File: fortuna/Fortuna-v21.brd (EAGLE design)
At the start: 66 x 55.9 mm, 41 parts, among them J1 5V, J2 GND, J3 A0, J4 A3, J5 A5, J6 D2, J7 *D5, J8 *D10, J9 VIN, M1 MOTOR20MM, M2 MOTOR20MM, Q1 PN2222A, Q2 PN2222A, U1 OPA2344, U2 OPA2344

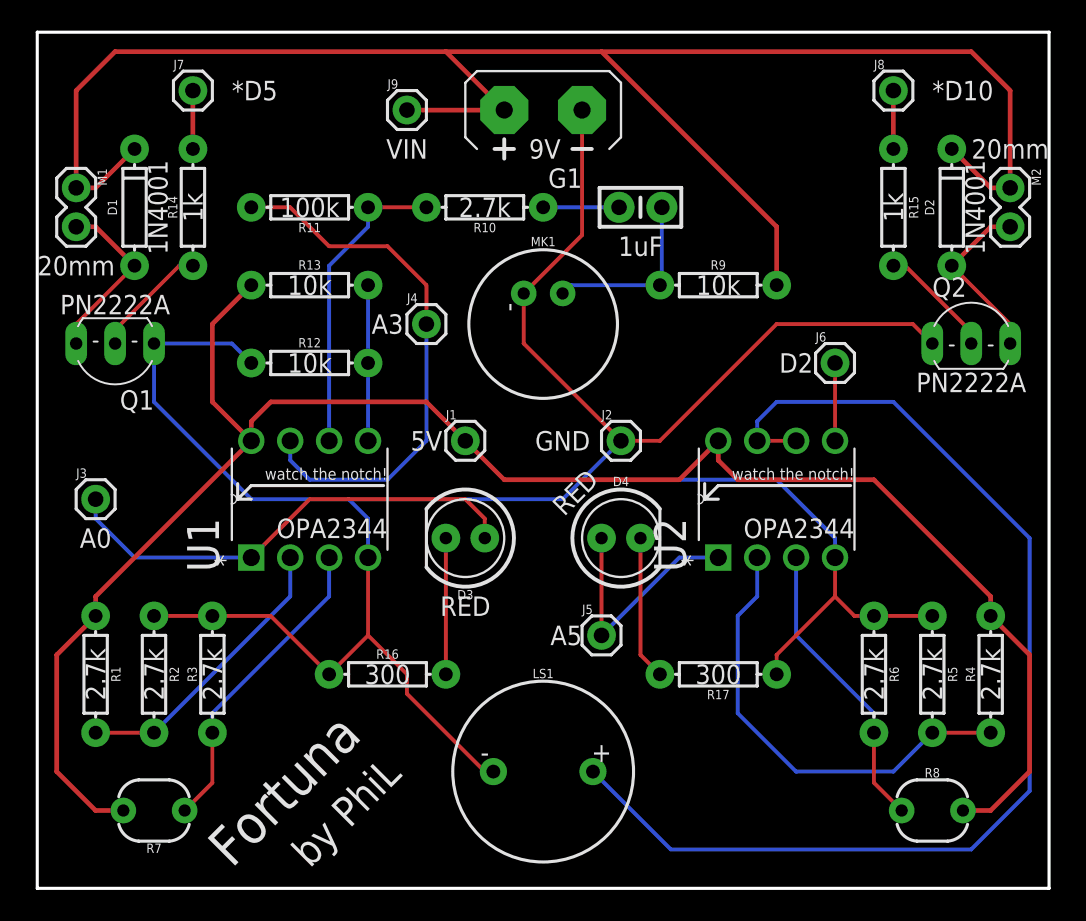
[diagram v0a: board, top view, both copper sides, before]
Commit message: Merge two OPA2344's into one OPA4344 & Add SPDT power switch
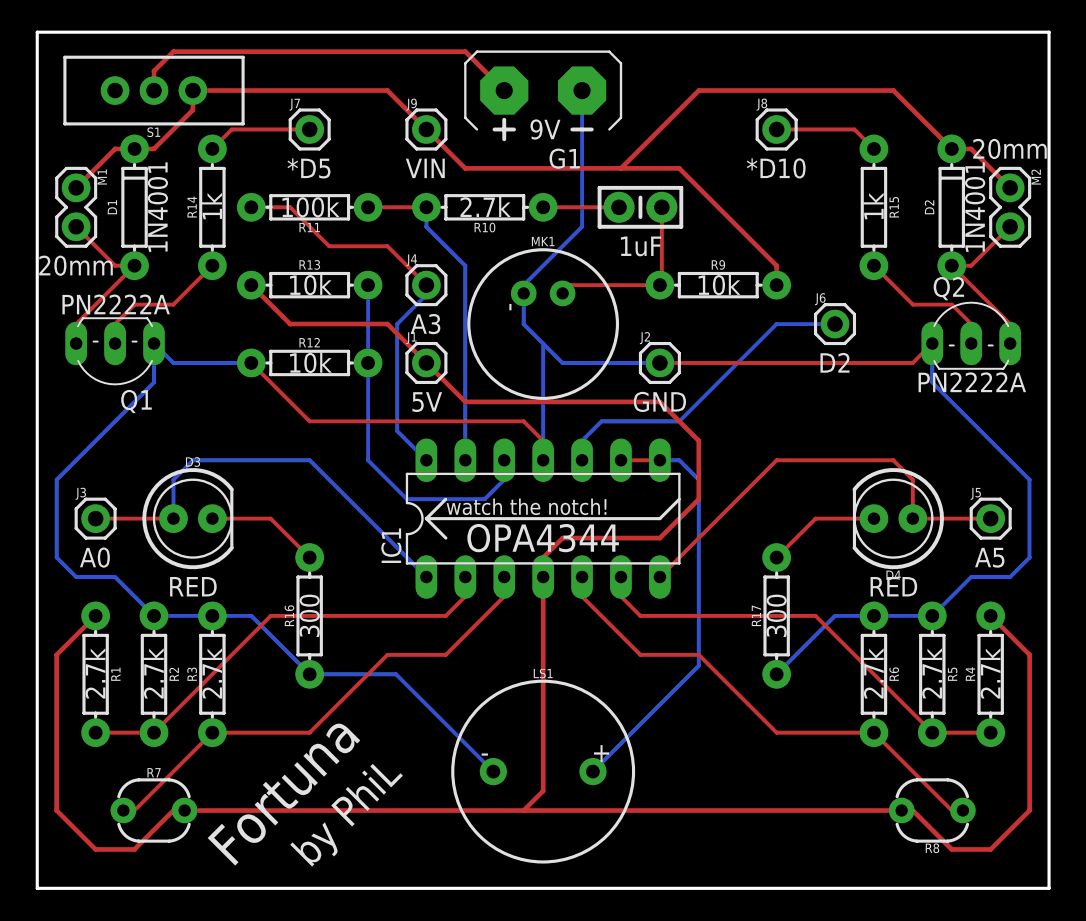
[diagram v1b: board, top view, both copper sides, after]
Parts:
- removed U1, U2: OPA2344, TexasInstruments:DIP254P762X508-8
- added IC1: OPA4340P, burr-brown:DIL14
- added S1: POWER_SWITCH, SparkFun-Switches:SWITCH_SPDT_PTH_11.6X4.0MM
- D1, D2: value 200mA/100V/1V -> 1N4001
- moved J5 26.5 mm to (62.2, 24.1)
- moved D3 17.8 mm to (10.2, 24.1), turned to 0 degrees
- moved D4 17.8 mm to (55.9, 24.1), turned to 180 degrees
- moved J8 8.03 mm to (48.3, 49.5)
- moved J7 8.03 mm to (17.8, 49.5)
- moved R16 6.35 mm to (17.8, 17.8), turned to 90 degrees
- moved J1 5.68 mm to (25.4, 34.3)
- moved J2 5.68 mm to (40.6, 34.3)
- moved R17 5.39 mm to (48.3, 17.8), turned to 90 degrees
- moved J4 2.54 mm to (25.4, 39.4)
- moved J6 2.54 mm to (52.1, 36.8)
- moved J9 1.80 mm to (25.4, 49.5)
- moved G1 1.27 mm to (33.0, 52.1)
- moved R15 1.27 mm to (54.6, 44.5)
- moved J3 1.27 mm to (3.81, 24.1)
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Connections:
- net *D10 renamed OUT_RMOTOR
- net *D5 renamed OUT_LMOTOR
- removed net A0: D3.A, J3.1, U1.1
- removed net A3: J4.1, R11.P$2, U1.7
- removed net A5: D4.A, J5.1, U2.1
- new net 9V: G1.+, S1.2
- new net OUT_LPHOTO: D3.A, IC1.1, J3.1
- new net OUT_MIC: IC1.14, J4.1, R11.P$2
- new net OUT_RPHOTO: D4.A, IC1.7, J5.1
- net +LPHOTO: now also IC1.3; no longer U1.3
- net +MIC: now also IC1.12; no longer U1.5
- net +RPHOTO: now also IC1.5; no longer U2.3
- net -LPHOTO: now also IC1.2; no longer U1.2
- net -MIC: now also IC1.13; no longer U1.6
- net -RPHOTO: now also IC1.6; no longer U2.2
- net 5V: now also IC1.4; no longer U1.8, U2.8
- net D2: now also IC1.10; no longer U2.5
- net GND: now also IC1.11; no longer U1.4, U2.4
- net OUT_BUZZER: now also IC1.8, IC1.9; no longer U2.6, U2.7
- net VIN: now also S1.3; no longer G1.+
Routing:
- net OUT_BUZZER: track 74.5 -> 27.5 mm
- net 5V: track 120.6 -> 161.2 mm
- net A3: track 35.4 -> 0.00 mm
- net VIN: track 117.2 -> 85.2 mm
- net A0: track 31.1 -> 0.00 mm
- net OUT_RPHOTO: track 0.00 -> 27.8 mm
- net OUT_LPHOTO: track 0.00 -> 27.8 mm
- net OUT_MIC: track 0.00 -> 26.5 mm
- net 9V: track 0.00 -> 25.7 mm
- net A5: track 16.1 -> 0.00 mm
- net D2: track 5.08 -> 20.9 mm
- net +MIC: track 10.2 -> 23.2 mm
- net +RPHOTO: track 19.4 -> 31.9 mm
- net +LPHOTO: track 20.4 -> 31.9 mm
- net -LPHOTO: track 18.9 -> 29.1 mm
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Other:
- board text added: "OPA4344"
- board text removed: "OPA2344"

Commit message: Fillet corners of the boards
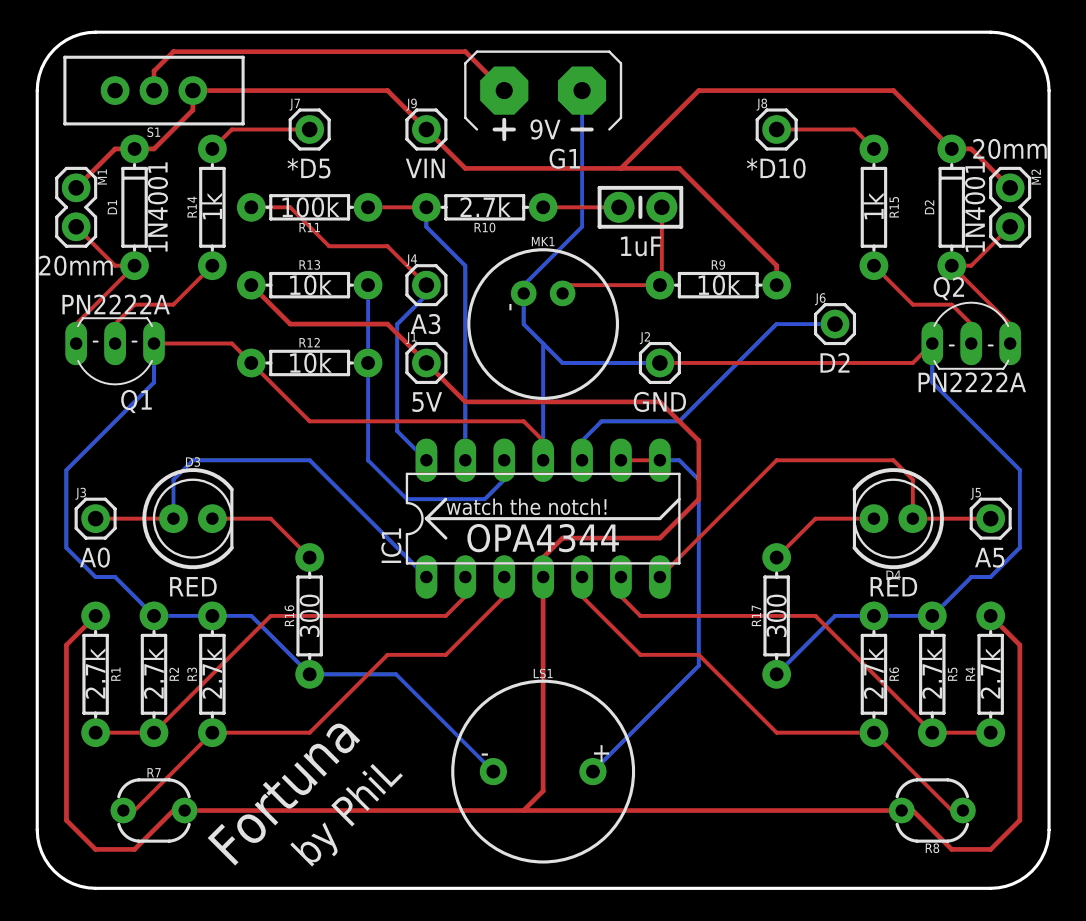
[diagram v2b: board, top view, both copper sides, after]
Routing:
- net GND: track 169.1 -> 166.6 mm
- net 5V: track 161.2 -> 160.2 mm
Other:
- outline, holes or cut-outs redrawn
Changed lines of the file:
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@@
 <board>
 <plain>
-<wire x1="0" y1="0" x2="0" y2="55.88" width="0.2032" layer="20"/>
-<wire x1="0" y1="55.88" x2="66.04" y2="55.88" width="0.2032" layer="20"/>
-<wire x1="66.04" y1="55.88" x2="66.04" y2="0" width="0.2032" layer="20"/>
-<wire x1="66.04" y1="0" x2="0" y2="0" width="0.2032" layer="20"/>
+<wire x1="0" y1="3.81" x2="0" y2="52.07" width="0.2032" layer="20"/>
+<wire x1="3.81" y1="55.88" x2="62.23" y2="55.88" width="0.2032" layer="20"/>
+<wire x1="66.04" y1="52.07" x2="66.04" y2="3.81" width="0.2032" layer="20"/>
 <text x="31.75" y="-7.62" size="1.778" layer="51" font="vector">Phi Luu</text>
 <text x="25.4" y="46.99" size="1.27" layer="21" font="vector" ratio="10" align="center">VIN</text>
@@
 <text x="22.86" y="11.43" size="2.54" layer="22" font="vector" ratio="15" rot="MR315">Fortuna</text>
 <text x="25.4" y="8.89" size="1.9304" layer="22" font="vector" ratio="15" rot="MR315">by PhiL</text>
+<wire x1="62.23" y1="0" x2="3.81" y2="0" width="0.2032" layer="20"/>
 <wire x1="25.4" y1="24.13" x2="26.67" y2="25.4" width="0.2032" layer="21"/>
 <wire x1="25.4" y1="24.13" x2="26.67" y2="22.86" width="0.2032" layer="21"/>
@@
 <wire x1="40.64" y1="24.13" x2="41.91" y2="25.4" width="0.2032" layer="21"/>
 <text x="33.02" y="22.86" size="1.778" layer="21" font="vector" ratio="15" align="center">OPA4344</text>
+<wire x1="66.04" y1="52.07" x2="62.23" y2="55.88" width="0.2032" layer="20" curve="90"/>
+<wire x1="66.04" y1="3.81" x2="62.23" y2="0" width="0.2032" layer="20" curve="-90"/>
+<wire x1="0" y1="3.81" x2="3.81" y2="0" width="0.2032" layer="20" curve="90"/>
+<wire x1="0" y1="52.07" x2="3.81" y2="55.88" width="0.2032" layer="20" curve="-90"/>
 </plain>
 <attributes>
@@
 <wire x1="33.02" y1="35.56" x2="34.29" y2="34.29" width="0.254" layer="16"/>
 <wire x1="34.29" y1="34.29" x2="40.64" y2="34.29" width="0.254" layer="16"/>
-<wire x1="13.97" y1="34.29" x2="8.89" y2="34.29" width="0.254" layer="16"/>
-<wire x1="8.89" y1="34.29" x2="7.62" y2="35.56" width="0.254" layer="16"/>
-<wire x1="7.62" y1="35.56" x2="7.62" y2="33.02" width="0.254" layer="16"/>
-<wire x1="7.62" y1="33.02" x2="1.27" y2="26.67" width="0.254" layer="16"/>
-<wire x1="1.27" y1="26.67" x2="1.27" y2="21.59" width="0.254" layer="16"/>
-<wire x1="1.27" y1="21.59" x2="2.54" y2="20.32" width="0.254" layer="16"/>
-<wire x1="2.54" y1="20.32" x2="5.08" y2="20.32" width="0.254" layer="16"/>
-<wire x1="5.08" y1="20.32" x2="7.62" y2="17.78" width="0.254" layer="16"/>
-<wire x1="58.42" y1="35.56" x2="58.42" y2="33.02" width="0.254" layer="16"/>
-<wire x1="58.42" y1="33.02" x2="64.77" y2="26.67" width="0.254" layer="16"/>
-<wire x1="64.77" y1="26.67" x2="64.77" y2="21.59" width="0.254" layer="16"/>
-<wire x1="64.77" y1="21.59" x2="63.5" y2="20.32" width="0.254" layer="16"/>
-<wire x1="63.5" y1="20.32" x2="60.96" y2="20.32" width="0.254" layer="16"/>
-<wire x1="60.96" y1="20.32" x2="58.42" y2="17.78" width="0.254" layer="16"/>
-<wire x1="7.62" y1="17.78" x2="11.43" y2="17.78" width="0.254" layer="16"/>
+<wire x1="7.62" y1="33.02" x2="7.62" y2="35.56" width="0.254" layer="16"/>
+<wire x1="58.42" y1="33.02" x2="58.42" y2="35.56" width="0.254" layer="16"/>
+<wire x1="58.42" y1="17.78" x2="60.96" y2="20.32" width="0.254" layer="16"/>
+<wire x1="11.43" y1="17.78" x2="7.62" y2="17.78" width="0.254" layer="16"/>
 <wire x1="58.42" y1="17.78" x2="54.61" y2="17.78" width="0.254" layer="16"/>
 <wire x1="11.43" y1="17.78" x2="13.97" y2="17.78" width="0.254" layer="16"/>
@@
 <wire x1="33.02" y1="29.21" x2="31.75" y2="30.48" width="0.254" layer="1"/>
 <wire x1="31.75" y1="30.48" x2="17.78" y2="30.48" width="0.254" layer="1"/>
-<wire x1="17.78" y1="30.48" x2="13.97" y2="34.29" width="0.254" layer="1"/>
+<wire x1="13.97" y1="34.29" x2="17.78" y2="30.48" width="0.254" layer="1"/>
 <wire x1="40.64" y1="34.29" x2="57.15" y2="34.29" width="0.254" layer="1"/>
 <wire x1="57.15" y1="34.29" x2="58.42" y2="35.56" width="0.254" layer="1"/>
+<wire x1="1.905" y1="27.305" x2="7.62" y2="33.02" width="0.254" layer="16"/>
+<wire x1="7.62" y1="17.78" x2="5.08" y2="20.32" width="0.254" layer="16"/>
+<wire x1="5.08" y1="20.32" x2="3.81" y2="20.32" width="0.254" layer="16"/>
+<wire x1="3.81" y1="20.32" x2="1.905" y2="22.225" width="0.254" layer="16"/>
+<wire x1="1.905" y1="22.225" x2="1.905" y2="27.305" width="0.254" layer="16"/>
+<wire x1="60.96" y1="20.32" x2="62.23" y2="20.32" width="0.254" layer="16"/>
+<wire x1="62.23" y1="20.32" x2="64.135" y2="22.225" width="0.254" layer="16"/>
+<wire x1="64.135" y1="22.225" x2="64.135" y2="27.305" width="0.254" layer="16"/>
+<wire x1="64.135" y1="27.305" x2="58.42" y2="33.02" width="0.254" layer="16"/>
+<wire x1="7.62" y1="35.56" x2="12.7" y2="35.56" width="0.254" layer="1"/>
+<wire x1="12.7" y1="35.56" x2="13.97" y2="34.29" width="0.254" layer="1"/>
 <polygon width="0.254" layer="1" isolate="0.3048">
-<vertex x="0" y="0"/>
-<vertex x="0" y="55.88"/>
-<vertex x="66.04" y="55.88"/>
-<vertex x="66.04" y="0"/>
+<vertex x="0" y="3.81"/>
+<vertex x="0" y="52.07" curve="-90"/>
+<vertex x="3.81" y="55.88"/>
+<vertex x="62.23" y="55.88" curve="-90"/>
+<vertex x="66.04" y="52.07"/>
+<vertex x="66.04" y="3.81" curve="-90"/>
+<vertex x="62.23" y="0"/>
+<vertex x="3.81" y="0" curve="-90"/>
 </polygon>
 </signal>
@@
 <wire x1="8.89" y1="5.08" x2="6.35" y2="2.54" width="0.3048" layer="1"/>
 <wire x1="6.35" y1="2.54" x2="3.81" y2="2.54" width="0.3048" layer="1"/>
-<wire x1="3.81" y1="2.54" x2="1.27" y2="5.08" width="0.3048" layer="1"/>
-<wire x1="1.27" y1="5.08" x2="1.27" y2="15.24" width="0.3048" layer="1"/>
-<wire x1="1.27" y1="15.24" x2="3.81" y2="17.78" width="0.3048" layer="1"/>
 <wire x1="22.86" y1="36.83" x2="25.4" y2="34.29" width="0.3048" layer="1"/>
 <wire x1="22.86" y1="36.83" x2="16.51" y2="36.83" width="0.3048" layer="1"/>
@@
 <wire x1="57.15" y1="5.08" x2="59.69" y2="2.54" width="0.3048" layer="1"/>
 <wire x1="59.69" y1="2.54" x2="62.23" y2="2.54" width="0.3048" layer="1"/>
-<wire x1="62.23" y1="2.54" x2="64.77" y2="5.08" width="0.3048" layer="1"/>
-<wire x1="64.77" y1="5.08" x2="64.77" y2="15.24" width="0.3048" layer="1"/>
-<wire x1="64.77" y1="15.24" x2="62.23" y2="17.78" width="0.3048" layer="1"/>
 <wire x1="25.4" y1="34.29" x2="27.94" y2="31.75" width="0.3048" layer="1"/>
 <wire x1="27.94" y1="31.75" x2="40.64" y2="31.75" width="0.3048" layer="1"/>
@@
 <wire x1="34.29" y1="22.86" x2="33.02" y2="21.59" width="0.3048" layer="1"/>
 <wire x1="33.02" y1="21.59" x2="33.02" y2="20.32" width="0.3048" layer="1"/>
+<wire x1="3.81" y1="2.54" x2="1.905" y2="4.445" width="0.3048" layer="1"/>
+<wire x1="1.905" y1="4.445" x2="1.905" y2="15.875" width="0.3048" layer="1"/>
+<wire x1="1.905" y1="15.875" x2="3.81" y2="17.78" width="0.3048" layer="1"/>
+<wire x1="62.23" y1="2.54" x2="64.135" y2="4.445" width="0.3048" layer="1"/>
+<wire x1="64.135" y1="4.445" x2="64.135" y2="15.875" width="0.3048" layer="1"/>
+<wire x1="64.135" y1="15.875" x2="62.23" y2="17.78" width="0.3048" layer="1"/>
 </signal>
 <signal name="OUT_BUZZER">

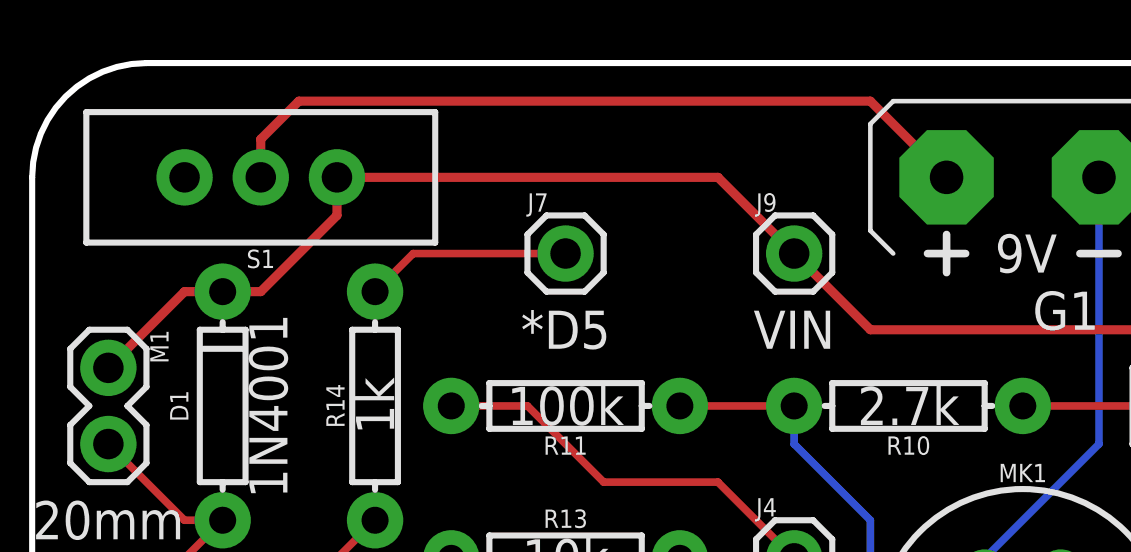
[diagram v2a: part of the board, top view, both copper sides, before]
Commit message: Change pin position SPDT slide switch
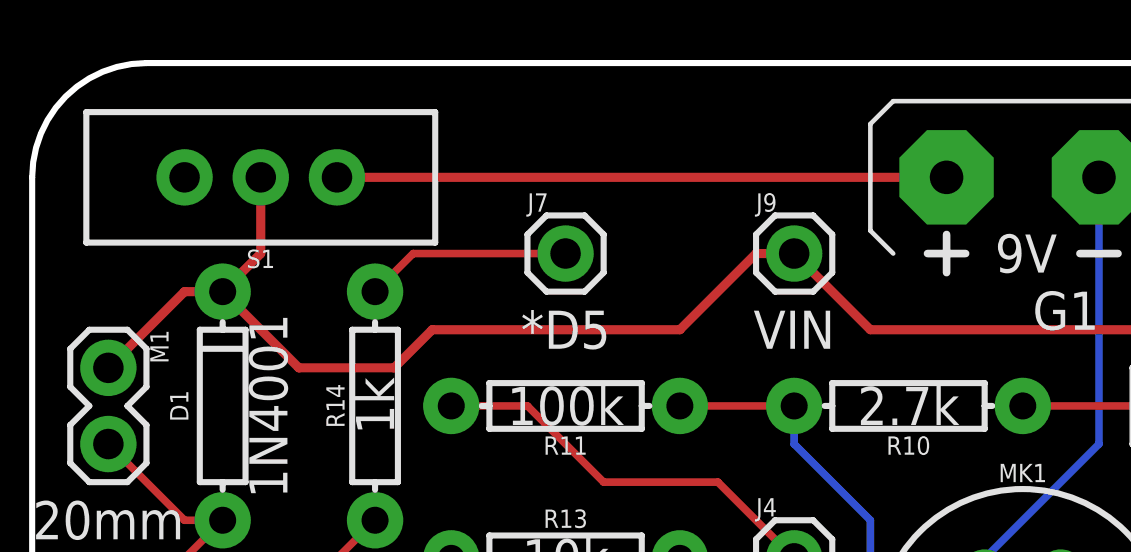
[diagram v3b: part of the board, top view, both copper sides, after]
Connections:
- net 9V: now also S1.3; no longer S1.2
- net VIN: now also S1.2; no longer S1.3
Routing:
- net 9V: track 25.7 -> 20.3 mm
- net VIN: track 85.2 -> 88.8 mm
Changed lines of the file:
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@@
 <contactref element="M1" pad="1"/>
 <contactref element="R9" pad="P$2"/>
-<contactref element="S1" pad="3"/>
 <contactref element="J9" pad="1"/>
-<wire x1="22.86" y1="52.07" x2="10.16" y2="52.07" width="0.3048" layer="1"/>
-<wire x1="22.86" y1="52.07" x2="25.4" y2="49.53" width="0.3048" layer="1"/>
-<wire x1="10.16" y1="52.07" x2="10.16" y2="50.8" width="0.3048" layer="1"/>
-<wire x1="10.16" y1="50.8" x2="7.62" y2="48.26" width="0.3048" layer="1"/>
-<wire x1="7.62" y1="48.26" x2="6.35" y2="48.26" width="0.3048" layer="1"/>
-<wire x1="6.35" y1="48.26" x2="5.08" y2="48.26" width="0.3048" layer="1"/>
+<wire x1="5.08" y1="48.26" x2="6.35" y2="48.26" width="0.3048" layer="1"/>
 <wire x1="5.08" y1="48.26" x2="2.54" y2="45.72" width="0.3048" layer="1"/>
 <wire x1="25.4" y1="49.53" x2="27.94" y2="46.99" width="0.3048" layer="1"/>
@@
 <wire x1="59.69" y1="48.26" x2="60.96" y2="48.26" width="0.3048" layer="1"/>
 <wire x1="60.96" y1="48.26" x2="63.5" y2="45.72" width="0.3048" layer="1"/>
+<contactref element="S1" pad="2"/>
+<wire x1="6.35" y1="48.26" x2="8.89" y2="45.72" width="0.3048" layer="1"/>
+<wire x1="8.89" y1="45.72" x2="12.065" y2="45.72" width="0.3048" layer="1"/>
+<wire x1="12.065" y1="45.72" x2="13.335" y2="46.99" width="0.3048" layer="1"/>
+<wire x1="13.335" y1="46.99" x2="21.59" y2="46.99" width="0.3048" layer="1"/>
+<wire x1="21.59" y1="46.99" x2="24.13" y2="49.53" width="0.3048" layer="1"/>
+<wire x1="24.13" y1="49.53" x2="25.4" y2="49.53" width="0.3048" layer="1"/>
+<wire x1="6.35" y1="48.26" x2="7.62" y2="49.53" width="0.3048" layer="1"/>
+<wire x1="7.62" y1="49.53" x2="7.62" y2="52.07" width="0.3048" layer="1"/>
 </signal>
 <signal name="N$1">
@@
 <wire x1="30.48" y1="26.67" x2="30.48" y2="27.94" width="0.254" layer="16"/>
 </signal>
-<signal name="9V" class="1">
+<signal name="9V">
 <contactref element="G1" pad="+"/>
-<contactref element="S1" pad="2"/>
-<wire x1="30.48" y1="52.07" x2="27.94" y2="54.61" width="0.3048" layer="1"/>
-<wire x1="27.94" y1="54.61" x2="8.89" y2="54.61" width="0.3048" layer="1"/>
-<wire x1="8.89" y1="54.61" x2="7.62" y2="53.34" width="0.3048" layer="1"/>
-<wire x1="7.62" y1="53.34" x2="7.62" y2="52.07" width="0.3048" layer="1"/>
+<contactref element="S1" pad="3"/>
+<wire x1="10.16" y1="52.07" x2="30.48" y2="52.07" width="0.3048" layer="1"/>
 </signal>
 </signals>
